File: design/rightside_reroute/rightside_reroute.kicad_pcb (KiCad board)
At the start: 4 copper layers, 144 x 95.7 mm, 198 parts, among them IC2 XC9148G50CER-G, IC3 nRF52833-QDAA-R7, IC4 74AHCT125PW,118, IC5 MCP23018T-E_SS, IC6 XC9291B33D1R-G, J1 USB_C_Receptacle_USB2.0_16P, J2 Battery Pos, J3 Battery Neg, J4 OLED_128x32, J6 Conn_01x04, J7 F32Q-1A7H1-11012, U2 BQ24072RGT, U3 USB6B1, U4 BQ27441-G1, U5 PEC11L-4015F-S0015, U6 PEC11L-4015F-S0015, Y1 ECS-320-8-37B2-JTY-TR

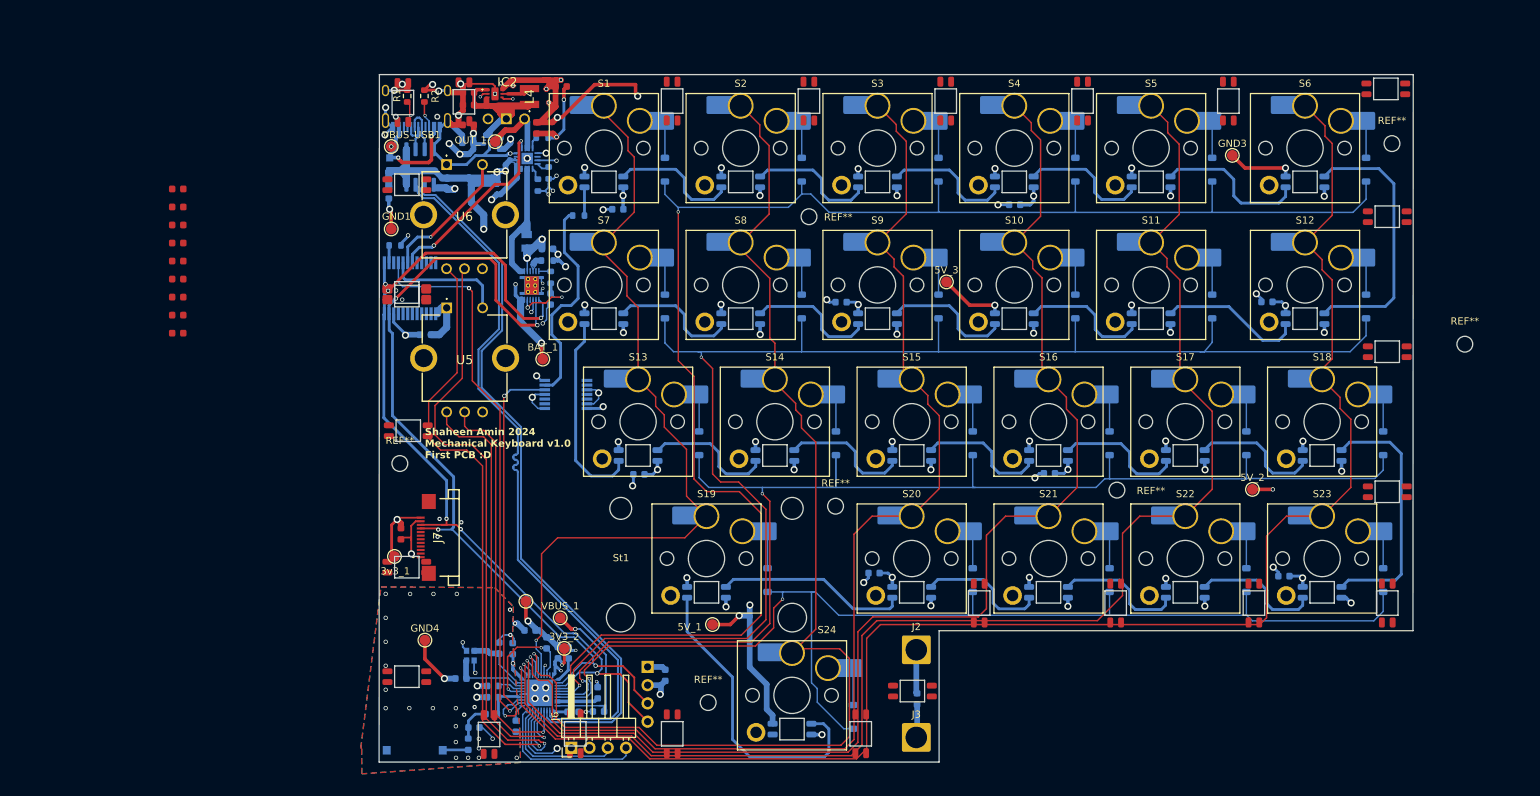
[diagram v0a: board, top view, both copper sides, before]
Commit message: reroute power input
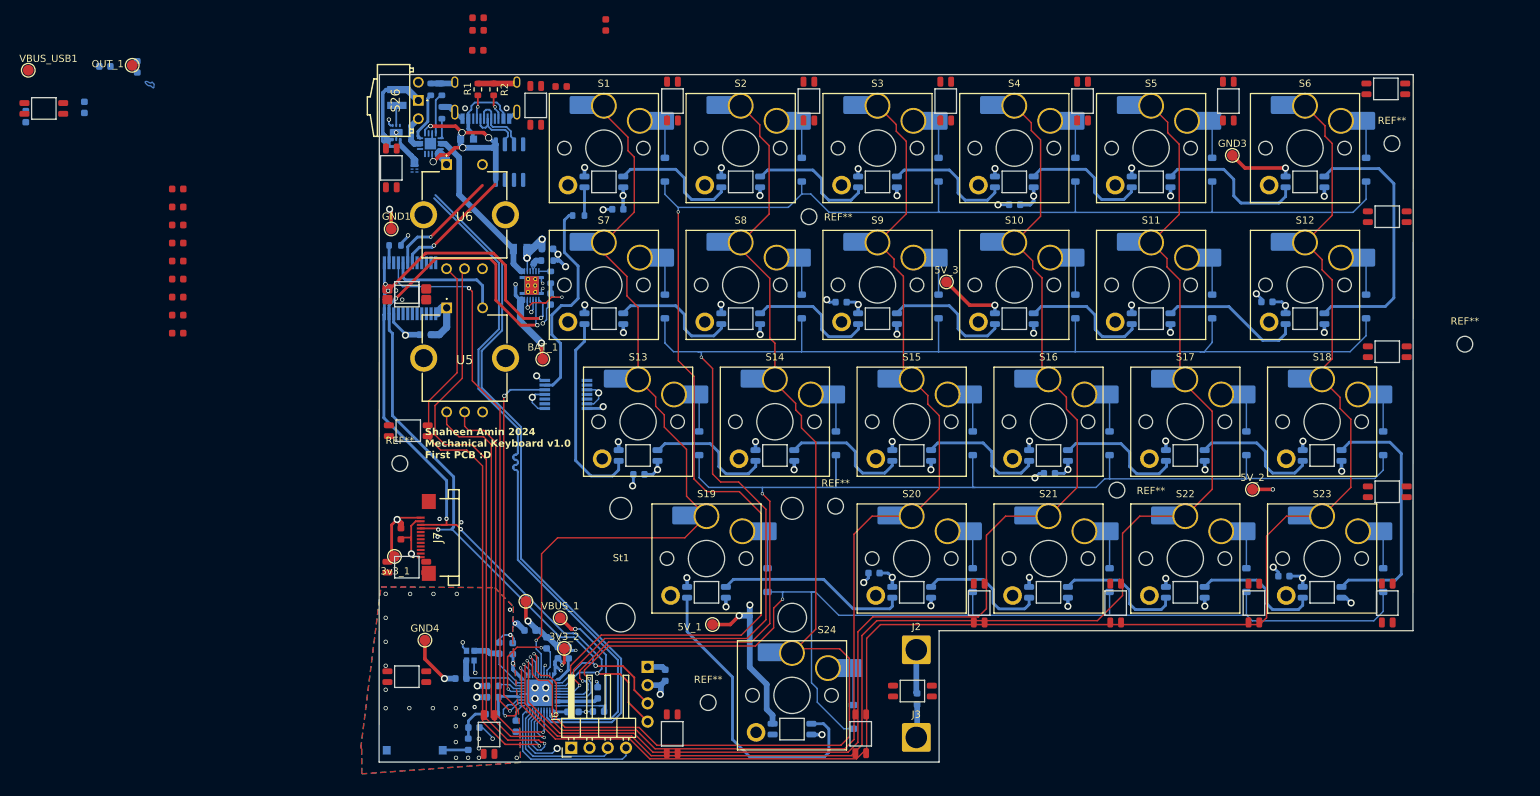
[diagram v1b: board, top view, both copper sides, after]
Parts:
- removed D50: LED_SK6812MINI, ScottoKeebs_Components:LED_SK6812MINI
- IC2, L4: moved to B.Cu
- S26: moved to F.Cu
- moved D34 89.1 mm to (132.4, 40.8)
- moved C24 51.7 mm to (50.5, 41.7)
- moved L3 51.7 mm to (57.9, 36.1)
- moved C40 51.7 mm to (53.4, 36.0)
- moved D26 51.7 mm to (44.9, 41.9)
- moved OUT_1 51.7 mm to (57.2, 35.9)
- moved VBUS_USB1 51.7 mm to (42.7, 36.5)
- moved C23 51.7 mm to (42.4, 43.0)
- moved R4 18.9 mm to (100.3, 39.2), turned to 90 degrees
- moved L4 18.5 mm to (94.0, 40.3), turned to -90 degrees
- moved C26 17.3 mm to (123.1, 30.2)
- moved R3 16.9 mm to (98.7, 39.2), turned to -90 degrees
- moved R5 16.7 mm to (100.3, 42.5), turned to -90 degrees
- moved IC2 14.8 mm to (93.9, 45.2), turned to 90 degrees
- moved U2 13.6 mm to (98.7, 46.8), turned to 180 degrees
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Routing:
- net GND: track 230.5 -> 163.6 mm, vias 107 -> 88
- net 5V: track 123.2 -> 81.8 mm, vias 35 -> 28
- net /VBUS: track 74.2 -> 54.3 mm, vias 5 -> 6
- net 3V3: track 64.4 -> 51.5 mm, vias 14 -> 10
- net /CHG: track 26.5 -> 16.7 mm, vias 2 -> 1
- net Net-(IC2-BAT): track 37.0 -> 29.7 mm
- net Net-(U2-ILIM): track 1.67 -> 6.82 mm
- net /VBUS_USB: track 16.6 -> 11.5 mm, vias 3 -> 0
- net /OUT: track 9.85 -> 4.94 mm
- net /BAT_SRN: track 18.8 -> 23.0 mm
- net D-: track 100.6 -> 96.8 mm
- net Net-(U2-ISET): track 1.94 -> 5.75 mm
- net D+: track 100.7 -> 97.3 mm
- net Net-(IC2-LX): track 5.98 -> 2.83 mm
- net /NO2: track 19.1 -> 16.2 mm
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
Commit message: begin making space for led near switch
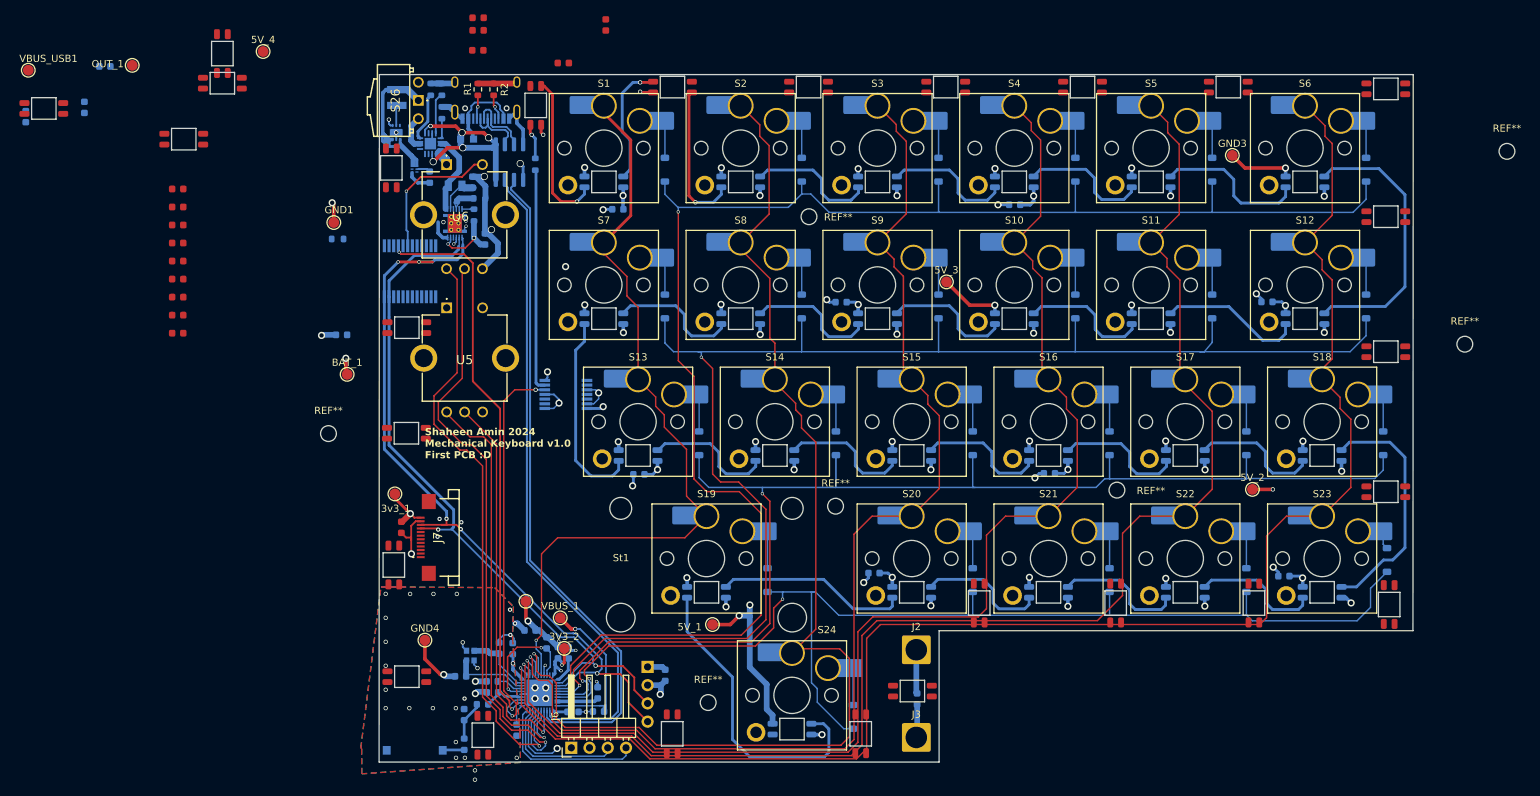
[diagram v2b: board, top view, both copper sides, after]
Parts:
- added 5V_4: TestPoint, TestPoint:TestPoint_Pad_D1.5mm, F.Cu at (75.4, 33.9)
- added D25: LED_SK6812MINI, ScottoKeebs_Components:LED_SK6812MINI, F.Cu at (69.7, 34.2)
- added D34: LED_SK6812MINI, ScottoKeebs_Components:LED_SK6812MINI, F.Cu at (69.7, 38.3)
- moved L3 43.5 mm to (98.6, 51.4)
- moved D27 37.7 mm to (64.4, 46.1)
- moved BAT_1 27.3 mm to (87.1, 78.9)
- moved REF** 16.0 mm to (248.6, 47.8)
- moved C18 14.0 mm to (104.6, 52.1), turned to 90 degrees
- moved R8 13.8 mm to (104.8, 56.7)
- moved U4 13.8 mm to (102.1, 57.9)
- moved R7 12.8 mm to (105.5, 54.4)
- moved R6 12.6 mm to (102.1, 52.6)
- moved C22 12.4 mm to (106.3, 60.0), turned to 90 degrees
- moved C20 11.7 mm to (86.3, 73.4)
- moved REF** 10.8 mm to (84.5, 87.1)
- moved R10 9.34 mm to (113.3, 49.6), turned to 90 degrees
- moved 3v3_1 8.71 mm to (93.8, 95.5)
- moved R9 8.05 mm to (85.8, 60.0)
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- renumbered D25 to D1, D1 to D2, D34 to D3, D2 to D4
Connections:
- D1 pad 2: Net-(D25-DOUT) -> Net-(D1-DOUT)
- D1 pad 4: Net-(D24-DOUT) -> Net-(D1-DIN)
- D2 pad 2: Net-(D1-DOUT) -> Net-(D2-DOUT)
- D2 pad 4: Net-(D1-DIN) -> Net-(D1-DOUT)
- D3 pad 2: Net-(D34-DOUT) -> Net-(D3-DOUT)
- D3 pad 4: Net-(D30-DOUT) -> Net-(D2-DOUT)
- D4 pad 2: Net-(D2-DOUT) -> Net-(D4-DOUT)
- D4 pad 4: Net-(D1-DOUT) -> Net-(D3-DOUT)
- D49 pad 2: Net-(D49-DOUT) -> unconnected-(D49-DOUT-Pad2)
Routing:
- net Net-(D3-DOUT): track 18.1 -> 39.0 mm, vias 0 -> 1
- net Net-(D2-DOUT): track 18.1 -> 35.5 mm, vias 0 -> 1
- net /SCL: track 118.1 -> 101.3 mm, vias 4 -> 2
- net /CHG: track 16.7 -> 0.00 mm, vias 1 -> 0
- net /NO: track 16.7 -> 0.00 mm
- net /SDA: track 123.1 -> 108.7 mm
- net /BAT: track 27.1 -> 15.0 mm, vias 4 -> 2
- net /BAT_SRN: track 23.0 -> 11.4 mm
- net GND: track 163.6 -> 172.3 mm, vias 88 -> 85
- net D-: track 96.8 -> 91.4 mm
- net 3V3: track 51.5 -> 46.4 mm, vias 10 -> 9
- net D+: track 97.3 -> 92.9 mm
- net Net-(D1-DOUT): track 18.1 -> 22.1 mm, vias 0 -> 1
- net /NO2: track 16.2 -> 19.8 mm
- net Net-(IC6-LX): track 0.00 -> 3.63 mm
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- removed copper zone on B.Cu, net /VBUS

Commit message: rerouting 3v3 transformer
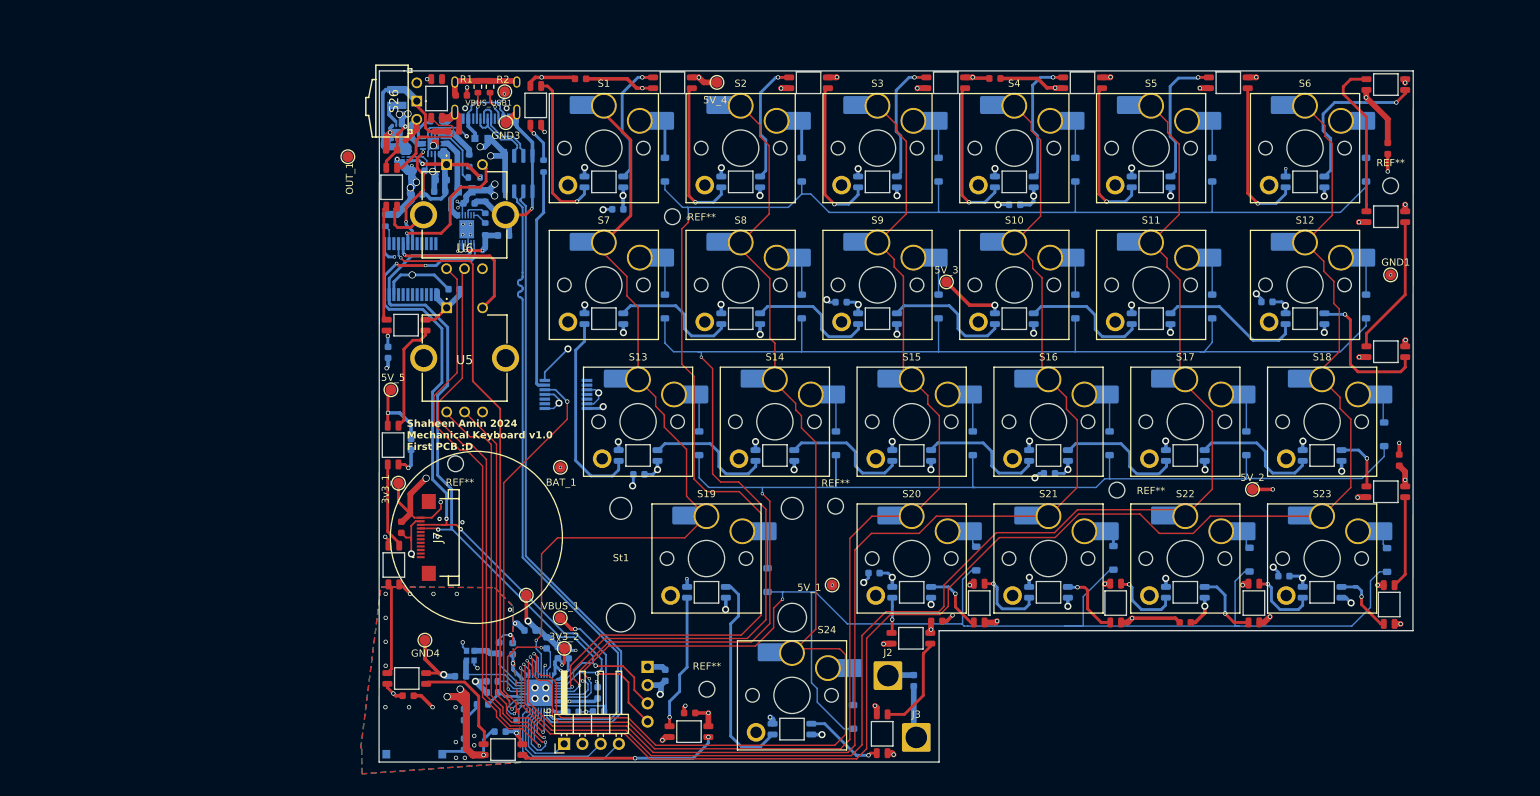
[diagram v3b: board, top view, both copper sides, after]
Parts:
- removed the D26 at (44.9, 41.9)
- removed the D27 at (64.4, 46.1)
- removed the D34 at (69.7, 38.3)
- removed the REF** at (84.5, 87.1)
- removed U4: BQ27441-G1, Package_SON:Texas_S-PDSO-N12
- added 5V_5: TestPoint, TestPoint:TestPoint_Pad_D1.5mm, F.Cu at (93.2, 81.0)
- added C46: 100nF, ScottoKeebs_Components:Capacitor_0603, B.Cu at (92.8, 75.8)
- added IC1: BQ27441DRZT-G1A, SamacSys_Parts:SON40P400X250X100-13N-D, B.Cu at (103.8, 58.7)
- C13, C38: moved to B.Cu
- moved C36 173.7 mm to (233.6, 90.8), turned to 90 degrees
- moved C35 168.6 mm to (232.0, 47.4), turned to -90 degrees
- moved REF** 152.7 mm to (102.2, 91.3)
- moved C43 147.4 mm to (203.8, 113.4)
- moved GND1 147.3 mm to (232.4, 65.0)
- moved REF** 119.2 mm to (232.4, 52.6)
- moved C41 116.6 mm to (177.3, 37.7)
- moved REF** 116.0 mm to (137.2, 122.7)
- moved C44 113.9 mm to (169.2, 113.2)
- moved GND3 101.3 mm to (109.2, 43.8)
- moved C45 88.8 mm to (134.8, 126.0), turned to 180 degrees
- moved C38 83.6 mm to (108.4, 128.6)
- moved C39 70.7 mm to (95.6, 123.6)
- moved C40 67.7 mm to (96.0, 88.6), turned to 90 degrees
- moved VBUS_USB1 66.4 mm to (109.1, 39.5)
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- renumbered D5 to D10, D46 to D11, D6 to D12, D45 to D13, D44 to D14, D43 to D15, D7 to D16, D8 to D17, D9 to D18, D10 to D19, D11 to D20, D12 to D21, D13 to D22, D14 to D23, D15 to D24, D16 to D25, D17 to D26, D18 to D27, D42 to D28, D41 to D29, D19 to D30, D40 to D31, D20 to D32, D39 to D33, D21 to D34, D38 to D35, D22 to D36, D36 to D38, D24 to D39, D23 to D40, D35 to D41, D33 to D42, D32 to D43, D31 to D44, D29 to D45, D28 to D46, D30 to D47, D25 to D48, D49 to D5, D3 to D6, D48 to D7, D4 to D8, D47 to D9
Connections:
- C22 pad 1: Net-(U4-V_{DD}) -> /VDD
- C40 pad 2: 3V3 -> 5V
- D10 pad 2: Net-(D5-DOUT) -> Net-(D10-DOUT)
- D10 pad 4: Net-(D4-DOUT) -> Net-(D10-DIN)
- D11 pad 2: Net-(D46-DOUT) -> Net-(D11-DOUT)
- D11 pad 4: Net-(D42-DOUT) -> Net-(D10-DOUT)
- D12 pad 2: Net-(D6-DOUT) -> Net-(D12-DOUT)
- D12 pad 4: Net-(D5-DOUT) -> Net-(D11-DOUT)
- D13 pad 2: Net-(D45-DOUT) -> Net-(D13-DOUT)
- D13 pad 4: Net-(D41-DOUT) -> Net-(D12-DOUT)
- D14 pad 2: Net-(D40-DIN) -> Net-(D14-DOUT)
- D14 pad 4: Net-(D44-DIN) -> Net-(D13-DOUT)
- D15 pad 2: Net-(D39-DIN) -> Net-(D15-DOUT)
- D15 pad 4: Net-(D43-DIN) -> Net-(D14-DOUT)
- D16 pad 4: Net-(D6-DOUT) -> Net-(D15-DOUT)
- D27 pad 2: Net-(D18-DOUT) (its old number) -> Net-(D27-DOUT)
- D28 pad 2: Net-(D42-DOUT) -> Net-(D28-DOUT)
- D28 pad 4: Net-(D38-DOUT) -> Net-(D27-DOUT)
- D29 pad 2: Net-(D41-DOUT) -> Net-(D29-DOUT)
- D29 pad 4: Net-(D37-DOUT) -> Net-(D28-DOUT)
- D30 pad 2: Net-(D19-DOUT) (its old number) -> Net-(D30-DOUT)
- D30 pad 4: Net-(D18-DOUT) (its old number) -> Net-(D29-DOUT)
- D31 pad 2: Net-(D36-DIN) -> Net-(D31-DOUT)
- D31 pad 4: Net-(D40-DIN) -> Net-(D30-DOUT)
- D32 pad 2: Net-(D20-DOUT) (its old number) -> Net-(D32-DOUT)
- D32 pad 4: Net-(D19-DOUT) (its old number) -> Net-(D31-DOUT)
- D33 pad 2: Net-(D35-DIN) -> Net-(D33-DOUT)
- D33 pad 4: Net-(D39-DIN) -> Net-(D32-DOUT)
- D34 pad 2: Net-(D21-DOUT) (its old number) -> Net-(D34-DOUT)
- D34 pad 4: Net-(D20-DOUT) (its old number) -> Net-(D33-DOUT)
- D35 pad 2: Net-(D38-DOUT) -> Net-(D35-DOUT)
- D36 pad 2: Net-(D22-DOUT) (its old number) -> Net-(D36-DOUT)
- D36 pad 4: Net-(D21-DOUT) (its old number) -> Net-(D35-DOUT)
- D37 pad 4: Net-(D33-DOUT) -> Net-(D36-DOUT)
- D38 pad 2: Net-(D32-DIN) -> Net-(D38-DOUT)
- D38 pad 4: Net-(D36-DIN) -> Net-(D37-DOUT)
- D39 pad 2: Net-(D24-DOUT) (its old number) -> Net-(D39-DOUT)
- D39 pad 4: Net-(D23-DOUT) (its old number) -> Net-(D38-DOUT)
- D40 pad 2: Net-(D23-DOUT) (its old number) -> Net-(D40-DOUT)
- D40 pad 4: Net-(D22-DOUT) (its old number) -> Net-(D39-DOUT)
- D41 pad 2: Net-(D31-DIN) -> Net-(D41-DOUT)
- D41 pad 4: Net-(D35-DIN) -> Net-(D40-DOUT)
- D42 pad 2: Net-(D33-DOUT) -> Net-(D42-DOUT)
- D42 pad 4: Net-(D29-DOUT) -> Net-(D41-DOUT)
- D43 pad 2: Net-(D28-DIN) -> Net-(D43-DOUT)
- D43 pad 4: Net-(D32-DIN) -> Net-(D42-DOUT)
- D44 pad 2: Net-(D27-DIN) -> Net-(D44-DOUT)
- D44 pad 4: Net-(D31-DIN) -> Net-(D43-DOUT)
- D45 pad 2: Net-(D29-DOUT) -> Net-(D45-DOUT)
- D45 pad 4: Net-(D25-DOUT) (its old number) -> Net-(D44-DOUT)
- D46 pad 2: Net-(D28-DOUT) -> Net-(D46-DOUT)
- D46 pad 4: Net-(D28-DIN) -> Net-(D45-DOUT)
- D47 pad 2: Net-(D30-DOUT) -> Net-(D47-DOUT)
- D47 pad 4: Net-(D26-DOUT) (its old number) -> Net-(D46-DOUT)
- D48 pad 2: Net-(D25-DOUT) (its old number) -> unconnected-(D48-DOUT-Pad2)
- D48 pad 4: Net-(D24-DOUT) (its old number) -> Net-(D47-DOUT)
- D5 pad 2: unconnected-(D49-DOUT-Pad2) -> Net-(D5-DOUT)
- D5 pad 4: Net-(D28-DOUT) -> Net-(D4-DOUT)
- D6 pad 2: Net-(D3-DOUT) -> Net-(D6-DOUT)
- D6 pad 4: Net-(D2-DOUT) -> Net-(D5-DOUT)
- D7 pad 2: Net-(D44-DIN) -> Net-(D7-DOUT)
- D7 pad 4: Net-(D46-DOUT) -> Net-(D6-DOUT)
- D8 pad 2: Net-(D4-DOUT) -> Net-(D8-DOUT)
- D8 pad 4: Net-(D3-DOUT) -> Net-(D7-DOUT)
- D9 pad 2: Net-(D43-DIN) -> Net-(D10-DIN)
- D9 pad 4: Net-(D45-DOUT) -> Net-(D8-DOUT)
- R7 pad 1: Net-(U4-BIN) -> GND
- R7 pad 2: GND -> Net-(IC1-BIN)
- R8 pad 1: Net-(U4-GPOUT) -> /VDD
- R8 pad 2: Net-(U4-V_{DD}) -> Net-(IC1-GPOUT)
- U6 pad MH1: unconnected-(U6-PadMH1) -> GND
- U6 pad MH2: unconnected-(U6-PadMH2) -> GND
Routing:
- net GND: track 172.3 -> 293.7 mm, vias 85 -> 106
- net 5V: track 81.8 -> 161.2 mm, vias 28 -> 56
- net Net-(D23-DOUT) (its old number): track 43.0 -> 0.00 mm
- net 3V3: track 46.4 -> 82.0 mm, vias 9 -> 13
- net Net-(D18-DOUT) (its old number): track 33.8 -> 0.00 mm
- net Net-(D39-DOUT): track 0.00 -> 29.5 mm
- net Net-(D41-DOUT): track 0.00 -> 27.9 mm, vias 0 -> 2
- net Net-(D22-DOUT) (its old number): track 26.7 -> 0.00 mm
- net Net-(D12-DOUT): track 0.00 -> 22.6 mm, vias 0 -> 1
- net Net-(D13-DOUT): track 0.00 -> 22.4 mm
- net Net-(D11-DOUT): track 0.00 -> 22.0 mm, vias 0 -> 1
- net /Row 3: track 167.4 -> 189.3 mm
- net /NO: track 0.00 -> 21.7 mm, vias 0 -> 1
- net Net-(D10-DIN): track 0.00 -> 21.4 mm, vias 0 -> 1
- net Net-(D7-DOUT): track 0.00 -> 21.3 mm, vias 0 -> 1
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- removed copper zone on B.Cu, net Net-(U4-BIN)
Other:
- board size 144 x 95.7 mm -> 144 x 96.2 mm
